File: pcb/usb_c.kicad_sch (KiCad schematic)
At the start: 1 part, among them J3 12401826E412A

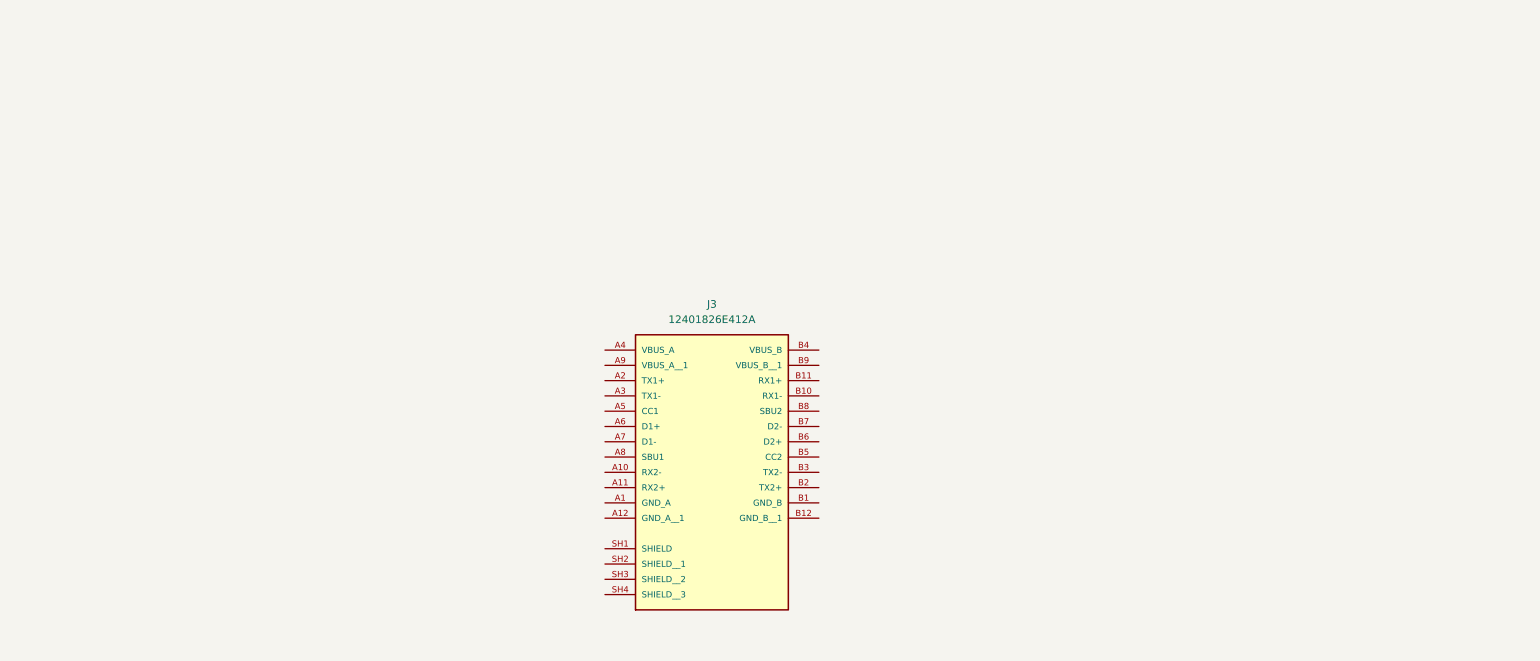
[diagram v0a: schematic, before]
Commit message: pcb: usb-c user connected
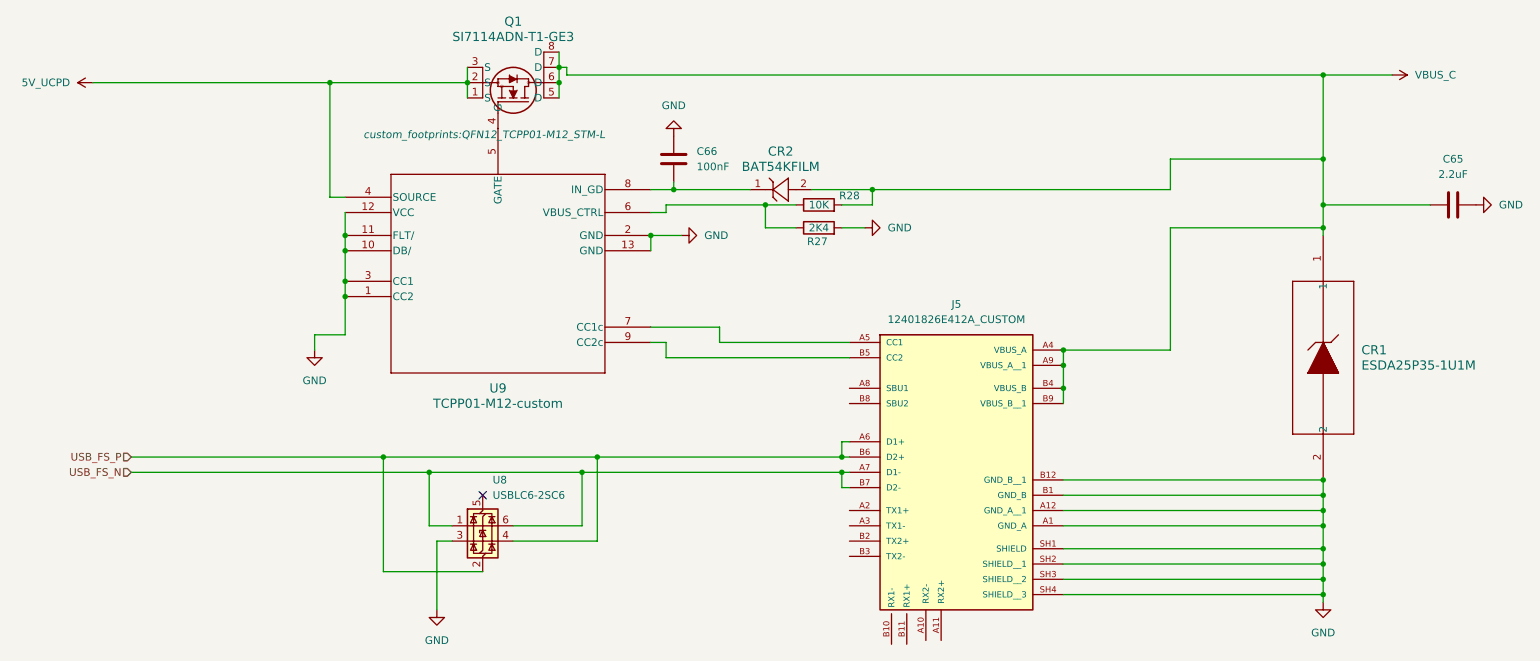
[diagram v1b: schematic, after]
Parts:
- removed J3: 12401826E412A, 12401826E412A:AMPHENOL_12401826E412A, symbol 12401826E412A:12401826E412A
- added C65: 2.2uF, symbol Device:C
- added C66: 100nF, symbol Device:C
- added CR1: ESDA25P35-1U1M, QFN1610_STM, symbol ESDA25P35-1U1M:ESDA25P35-1U1M
- added CR2: BAT54KFILM, SOD-523_STM, symbol BAT54KFILM:BAT54KFILM
- added J5: 12401826E412A_CUSTOM, 12401826E412A:AMPHENOL_12401826E412A, symbol 12401826E412A:12401826E412A_CUSTOM
- added Q1: SI7114ADN-T1-GE3, SON8_SI7615ADN-T1-GE3_VIS, symbol SI7114ADN-T1-GE3:SI7114ADN-T1-GE3
- added R27: 2K4, Resistor_THT:R_Array_SIP13, symbol Device:R
- added R28: 10K, Resistor_THT:R_Array_SIP13, symbol Device:R
- added U8: USBLC6-2SC6, Package_TO_SOT_SMD:SOT-23-6, symbol Power_Protection:USBLC6-2SC6
- added U9: TCPP01-M12-custom, custom_footprints:QFN12_TCPP01-M12_STM-L, symbol TCPP01-M12:TCPP01-M12-custom
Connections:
- new net: Q1.4 (G), U9.5 (GATE)
- new net: R27.1, R28.1, U9.6 (VBUS_CTRL)
- new net: J5.A5 (CC1), U9.7 (CC1c)
- new net: C66.2, CR2.1, U9.8 (IN_GD)
- new net: J5.B5 (CC2), U9.9 (CC2c)
- new net 5V_UCPD: Q1.1 (S), Q1.2 (S), Q1.3 (S), U9.4 (SOURCE)
- new net GND: C65.1, C66.1, CR1.2, J5.A1 (GND_A), J5.A12 (GND_A__1), J5.B1 (GND_B), J5.B12 (GND_B__1), J5.SH1 (SHIELD), J5.SH2 (SHIELD__1), J5.SH3 (SHIELD__2), J5.SH4 (SHIELD__3), R27.2, U8.3 (I/O2), U9.1 (CC2), U9.10 (DB/), U9.11 (FLT/), U9.12 (VCC), U9.13 (GND), U9.2 (GND), U9.3 (CC1)
- new net USB_FS_N: J5.A7 (D1-), J5.B7 (D2-), U8.1 (I/O1), U8.6 (I/O1)
- new net USB_FS_P: J5.A6 (D1+), J5.B6 (D2+), U8.2 (GND), U8.4 (I/O2)
- new net VBUS_C: C65.2, CR1.1, CR2.2, J5.A4 (VBUS_A), J5.A9 (VBUS_A__1), J5.B4 (VBUS_B), J5.B9 (VBUS_B__1), Q1.5 (D), Q1.6 (D), Q1.7 (D), Q1.8 (D), R28.2
- no-connect marks 0 -> 1

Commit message: pcb: changes usbc and add input power
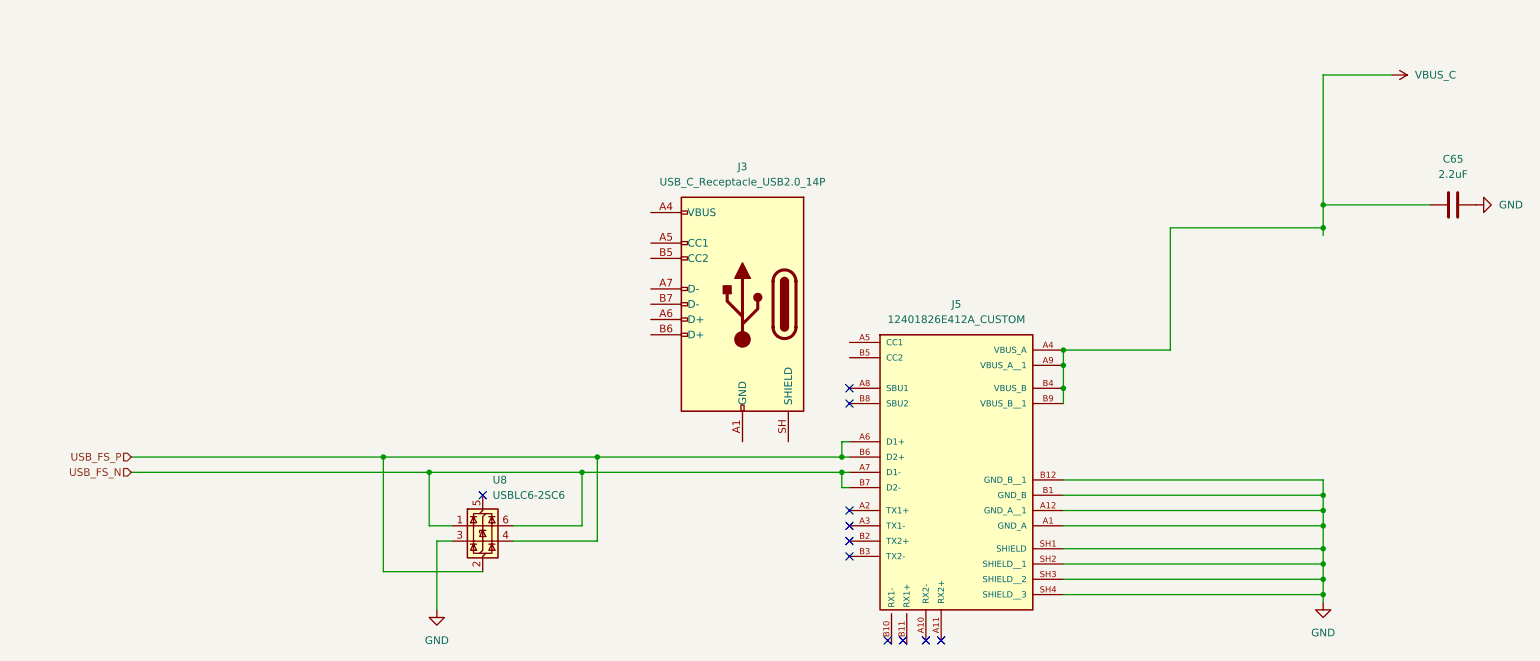
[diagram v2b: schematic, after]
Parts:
- removed C66: 100nF, symbol Device:C
- removed CR1: ESDA25P35-1U1M, QFN1610_STM, symbol ESDA25P35-1U1M:ESDA25P35-1U1M
- removed CR2: BAT54KFILM, SOD-523_STM, symbol BAT54KFILM:BAT54KFILM
- removed Q1: SI7114ADN-T1-GE3, SON8_SI7615ADN-T1-GE3_VIS, symbol SI7114ADN-T1-GE3:SI7114ADN-T1-GE3
- removed R27: 2K4, Resistor_THT:R_Array_SIP13, symbol Device:R
- removed R28: 10K, Resistor_THT:R_Array_SIP13, symbol Device:R
- removed U9: TCPP01-M12-custom, custom_footprints:QFN12_TCPP01-M12_STM-L, symbol TCPP01-M12:TCPP01-M12-custom
- added J3: USB_C_Receptacle_USB2.0_14P, symbol Connector:USB_C_Receptacle_USB2.0_14P
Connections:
- new net: J3.A1 (GND), J3.A12 (GND), J3.B1 (GND), J3.B12 (GND)
- new net: J3.A4 (VBUS), J3.A9 (VBUS), J3.B4 (VBUS), J3.B9 (VBUS)
- no-connect marks 1 -> 11
